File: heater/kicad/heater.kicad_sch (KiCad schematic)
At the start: 82 parts, among them J1 Conn_01x02_Pin, J2 Conn_01x02_Pin, J3 pcie_98, U1 OPA863SIDBVR, U11 ESD5344D-TP, U12 ESD5344D-TP, U13 XC6206P332MR, U15 TPS7A2025PDBVR, U2 D050505T-1WR4, U3 LTC1968, U4 LTC1968, U5 TPS72325DBVR, U8 ADS1115IDGS, U9 ISO1541

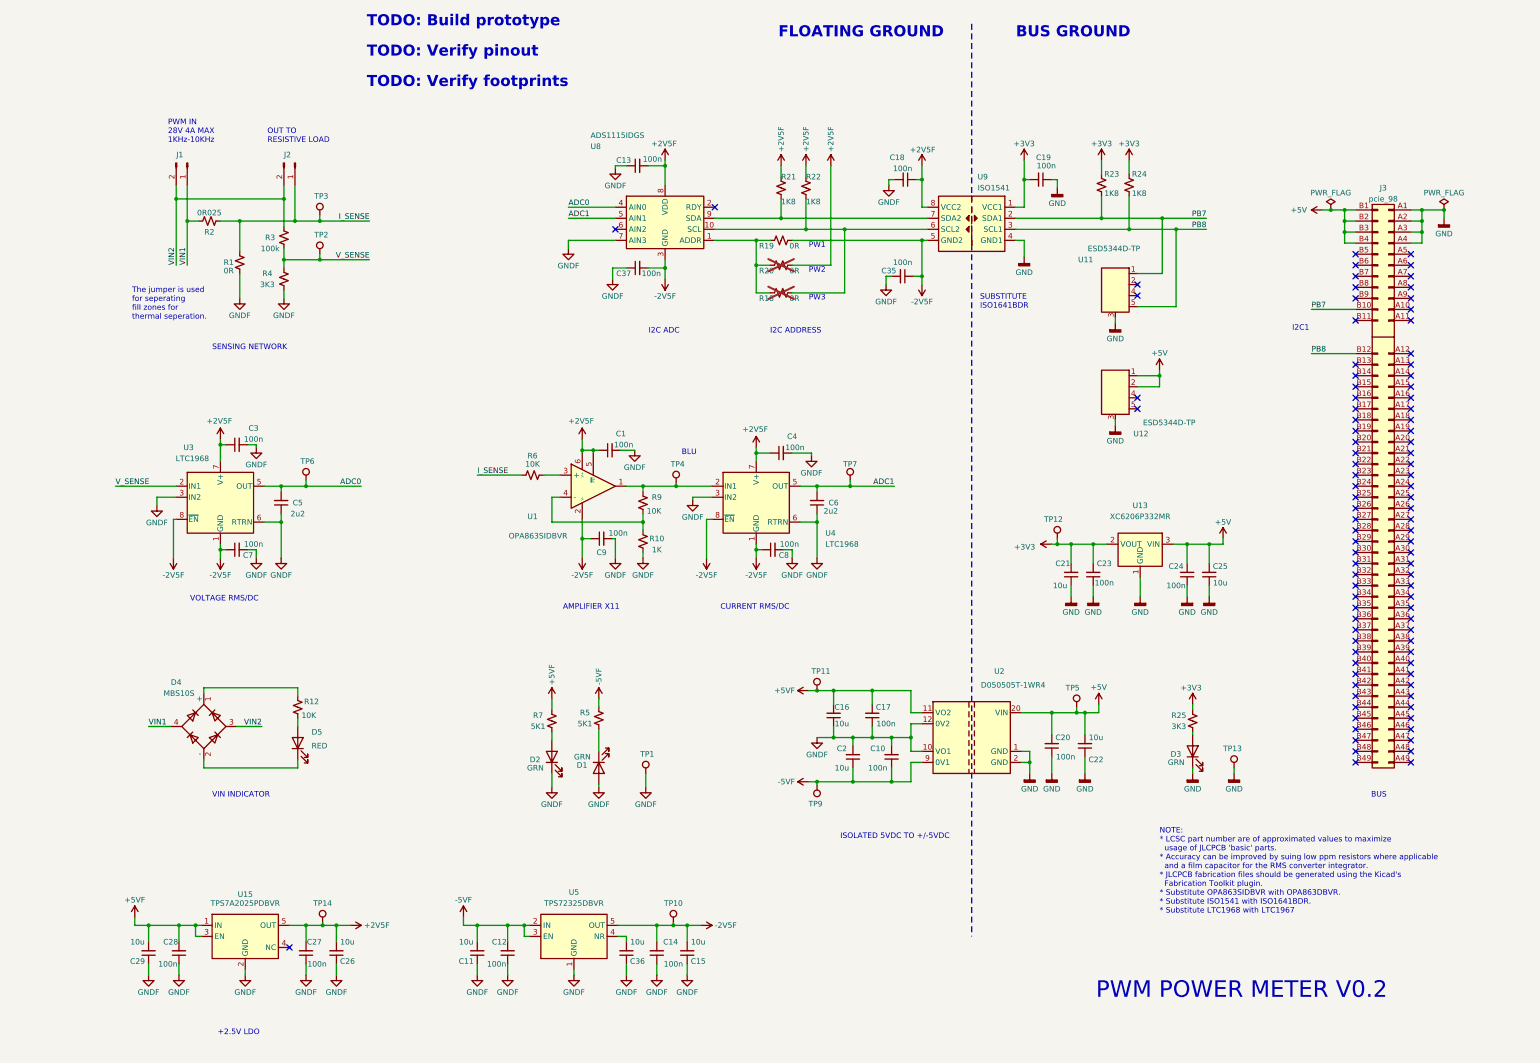
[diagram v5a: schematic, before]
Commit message: Updated the heater schematic.
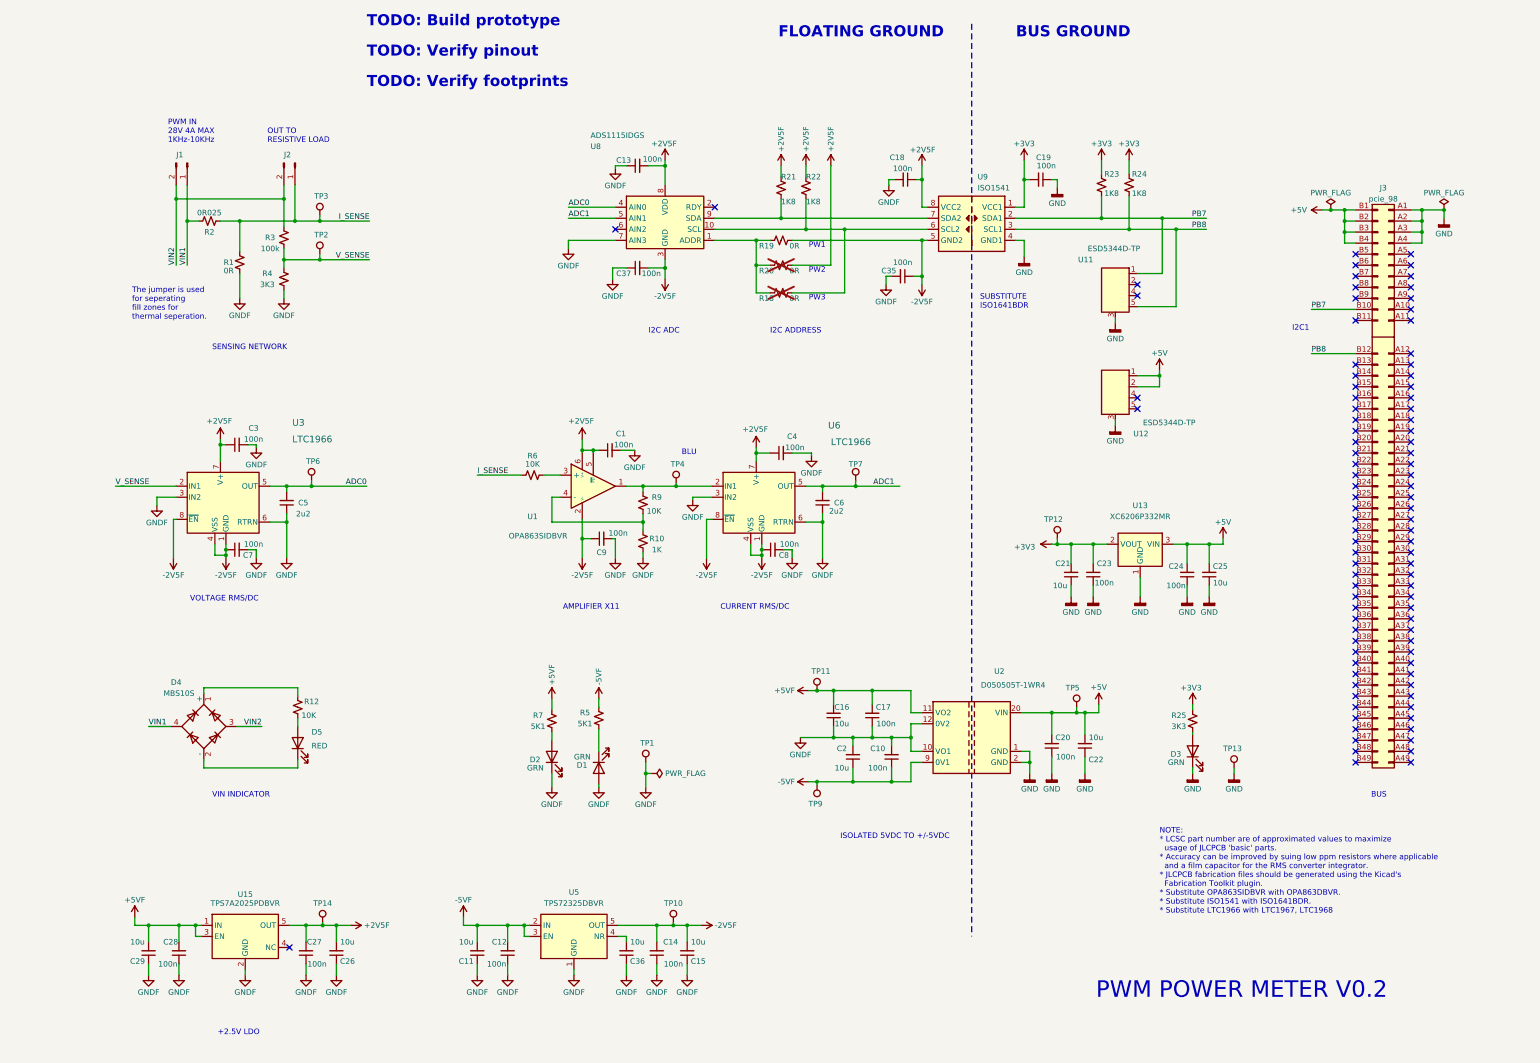
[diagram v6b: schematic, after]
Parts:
- removed U3, U4: LTC1968, Package_SO:MSOP-8_3x3mm_P0.65mm, symbol heater:LTC1968
- added U3, U6: LTC1966, Package_SO:MSOP-8_3x3mm_P0.65mm, symbol heater:LTC1966
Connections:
- net +2V5F: now also U3.7 (V+), U6.7 (V+)
- net -2V5F: now also U3.1 (GND), U3.4 (VSS), U3.8 (~{EN}), U6.1 (GND), U6.4 (VSS), U6.8 (~{EN})
- net ADC0: now also U3.5 (OUT)
- net ADC1: now also U6.5 (OUT)
- net GNDF: now also U3.3 (IN2), U3.6 (RTRN), U6.3 (IN2), U6.6 (RTRN)
- net V_SENSE: now also U3.2 (IN1)
- net at R9.1, TP4.1, U1.1: now also U6.2 (IN1)
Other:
- moved on the sheet: C5, C6, TP1, TP6, TP7

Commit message: Added series 0R resistors to the power supply rails.
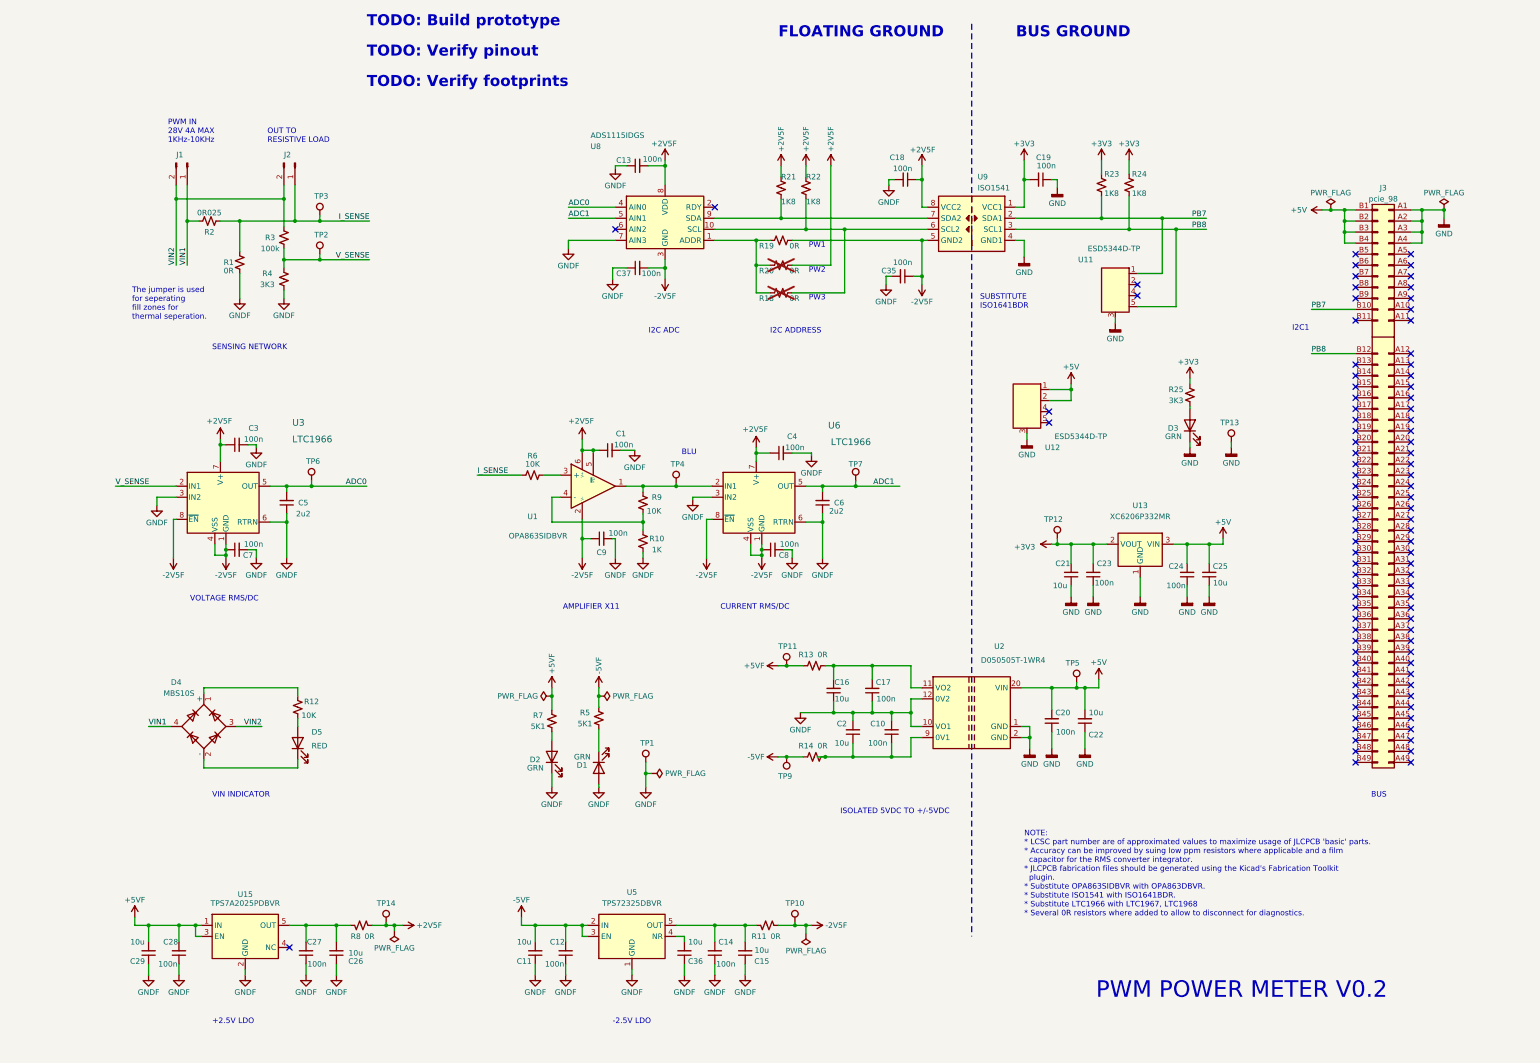
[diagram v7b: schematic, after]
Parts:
- added R11, R13, R14, R8: 0R, Resistor_SMD:R_0402_1005Metric, symbol Device:R_Small_US
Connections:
- net +2V5F: now also R8.1; no longer C26.2, C27.2, U15.5 (OUT)
- net +5VF: now also R13.2; no longer C16.2, C17.2, U2.11 (VO2)
- net -2V5F: now also R11.1; no longer C14.2, C15.2, U5.5 (OUT)
- net -5VF: now also R14.2; no longer C10.1, C2.1, U2.9 (0V1)
- new net: C16.2, C17.2, R13.1, U2.11 (VO2)
- new net: C26.2, C27.2, R8.2, U15.5 (OUT)
- new net: C14.2, C15.2, R11.2, U5.5 (OUT)
- new net: C10.1, C2.1, R14.1, U2.9 (0V1)
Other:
- note added: "-2.5V LDO"
- moved on the sheet: C10, C11, C12, C14, C15, C16, C17, C2, C20, C22, C36, D3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

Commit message: Cleaned up the sensing network.
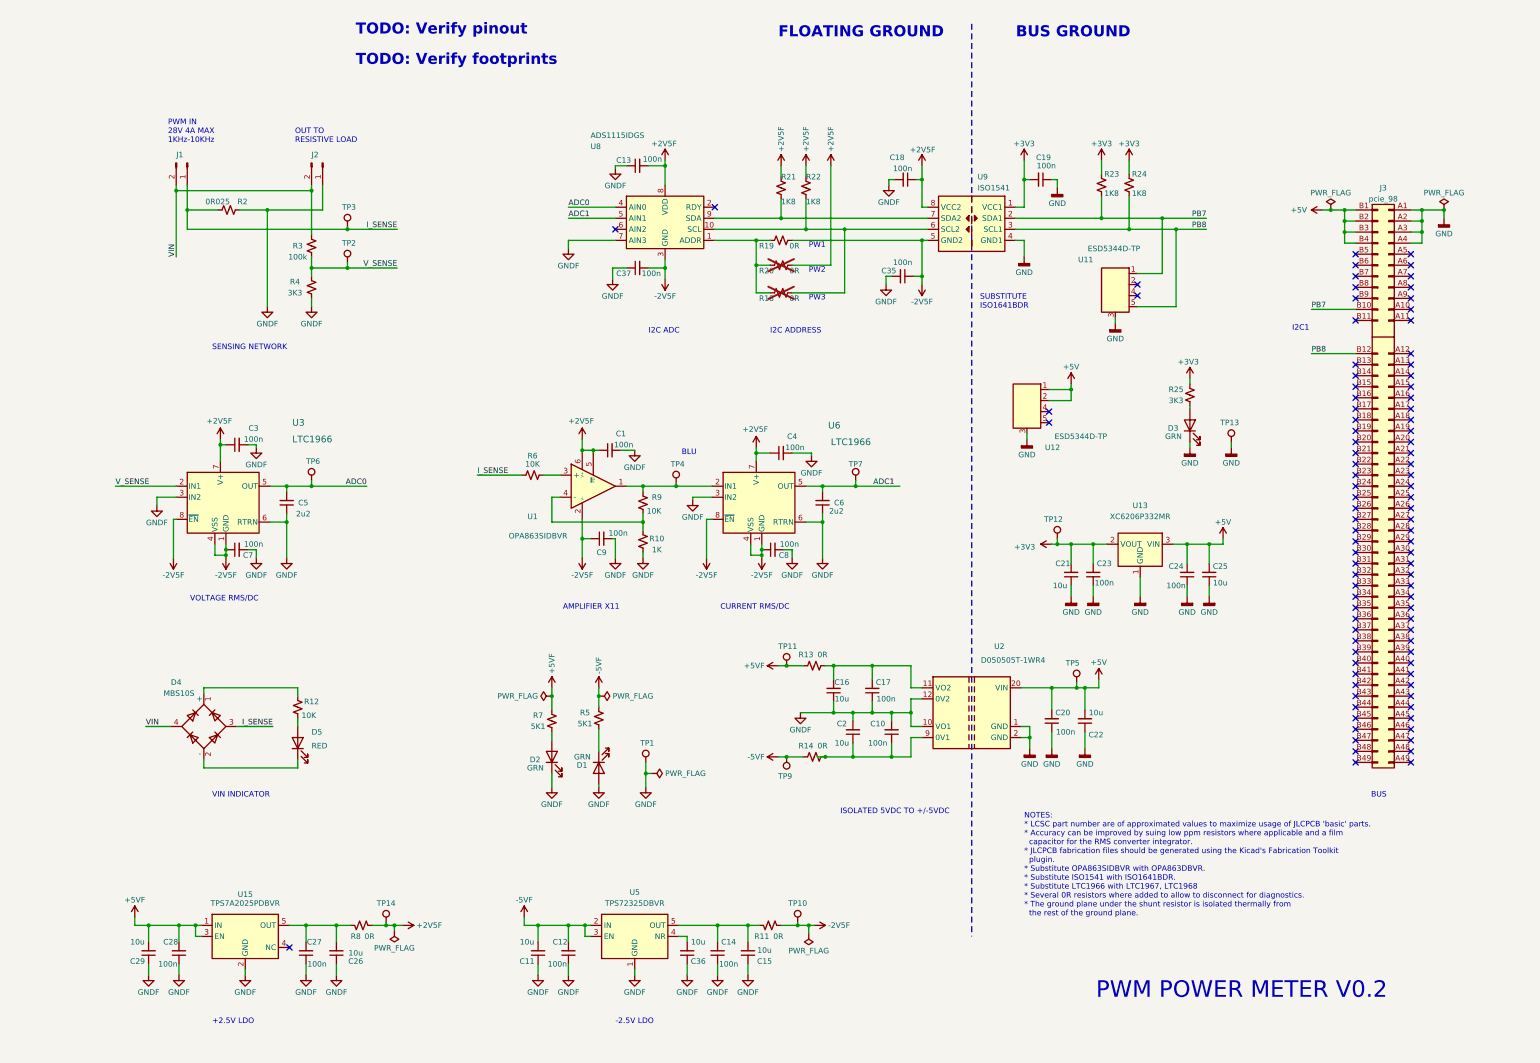
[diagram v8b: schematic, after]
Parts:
- removed R1: 0R, Resistor_SMD:R_0402_1005Metric, symbol Device:R_Small_US
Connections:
- net GNDF: now also J2.1 (Pin_1), R2.2
- net I_SENSE: now also D4.3, J1.1 (Pin_1), R2.1; no longer J2.1 (Pin_1), R2.2
- removed net VIN1: D4.4, J1.1 (Pin_1), R2.1
- net VIN2 renamed VIN
- net VIN: now also D4.4; no longer D4.3
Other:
- note added: "NOTES: * LCSC part number are of approximated values to maximize usage of JLCPCB 'basic' parts. * Accuracy can be improved by suing low ppm resistors where applicable and a film capacitor for the RMS converter integrator. * JLCPCB fabrication files should be generated using the Kicad's Fabrication Toolkit plugin. * Substitute OPA863SIDBVR with OPA863DBVR. * Substitute ISO1541 with ISO1641BDR. * S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"
- note removed: "NOTE: * LCSC part number are of approximated values to maximize usage of JLCPCB 'basic' parts. * Accuracy can be improved by suing low ppm resistors where applicable and a film capacitor for the RMS converter integrator. * JLCPCB fabrication files should be generated using the Kicad's Fabrication Toolkit plugin. * Substitute OPA863SIDBVR with OPA863DBVR. * Substitute ISO1541 with ISO1641BDR. * Su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"
- note removed: "TODO: Build prototype"
- note removed: "The jumper is used for seperating fill zones for thermal seperation."
- moved on the sheet: C11, C12, C14, C15, C36, J2, R11, R2, R3, R4, TP10, TP2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
